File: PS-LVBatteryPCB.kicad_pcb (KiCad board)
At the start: 2 copper layers, 23.4 x 39.7 mm, 10 parts, among them J1 NTC_01, J2 NTC_02, J3 NTC_OUT, J4 SUPP+, J5 SUPP_GND, J6 SUPP_FUSE

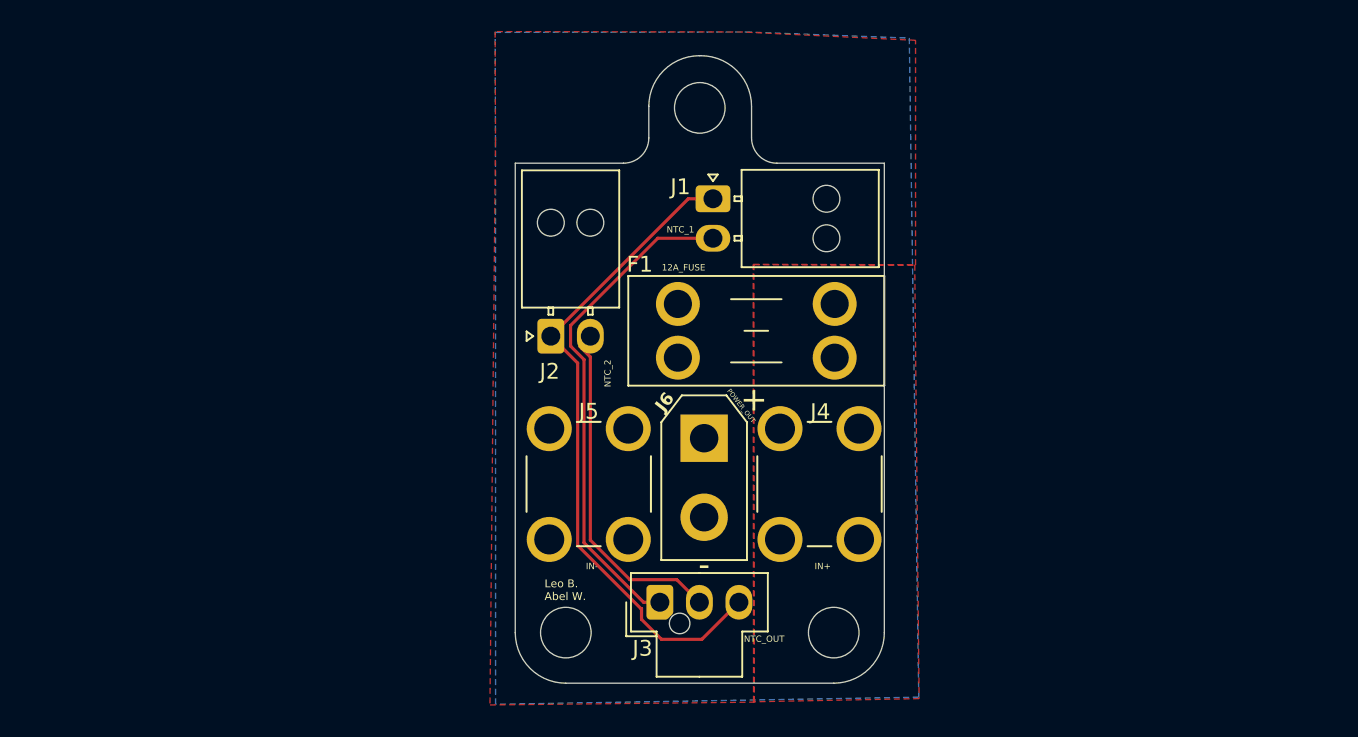
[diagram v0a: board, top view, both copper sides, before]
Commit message: redid layout for optimal terminal shape
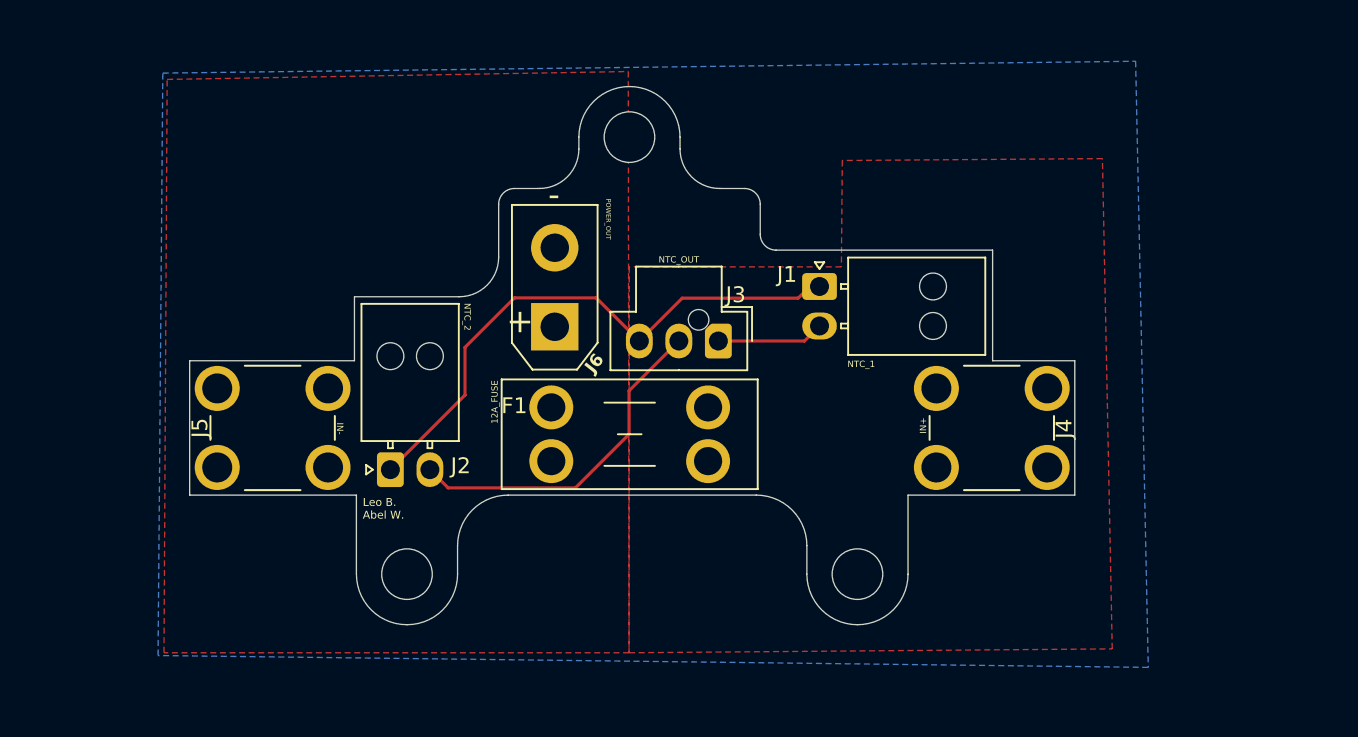
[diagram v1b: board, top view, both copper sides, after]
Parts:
- moved J5 20.3 mm to (171.1, 82.5), turned to 90 degrees
- moved J3 16.9 mm to (199.3, 77.0), turned to -90 degrees
- moved J2 13.2 mm to (178.6, 85.1)
- moved J6 11.8 mm to (188.9, 76.0), turned to 90 degrees
- moved J4 11.5 mm to (216.6, 82.5), turned to 90 degrees
- moved REF** 10.7 mm to (179.6, 91.7)
- moved F1 10.3 mm to (198.7, 84.5)
- moved J1 8.73 mm to (205.7, 73.5)
- moved REF** 4.82 mm to (193.7, 64.0)
- moved REF** 3.99 mm to (208.1, 91.7)
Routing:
- net Net-(J1-Pin_2): track 31.8 -> 6.79 mm
- net Net-(J1-Pin_1): track 41.8 -> 36.0 mm
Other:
- board size 23.4 x 39.7 mm -> 56 x 34.1 mm

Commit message: moved mounting holes
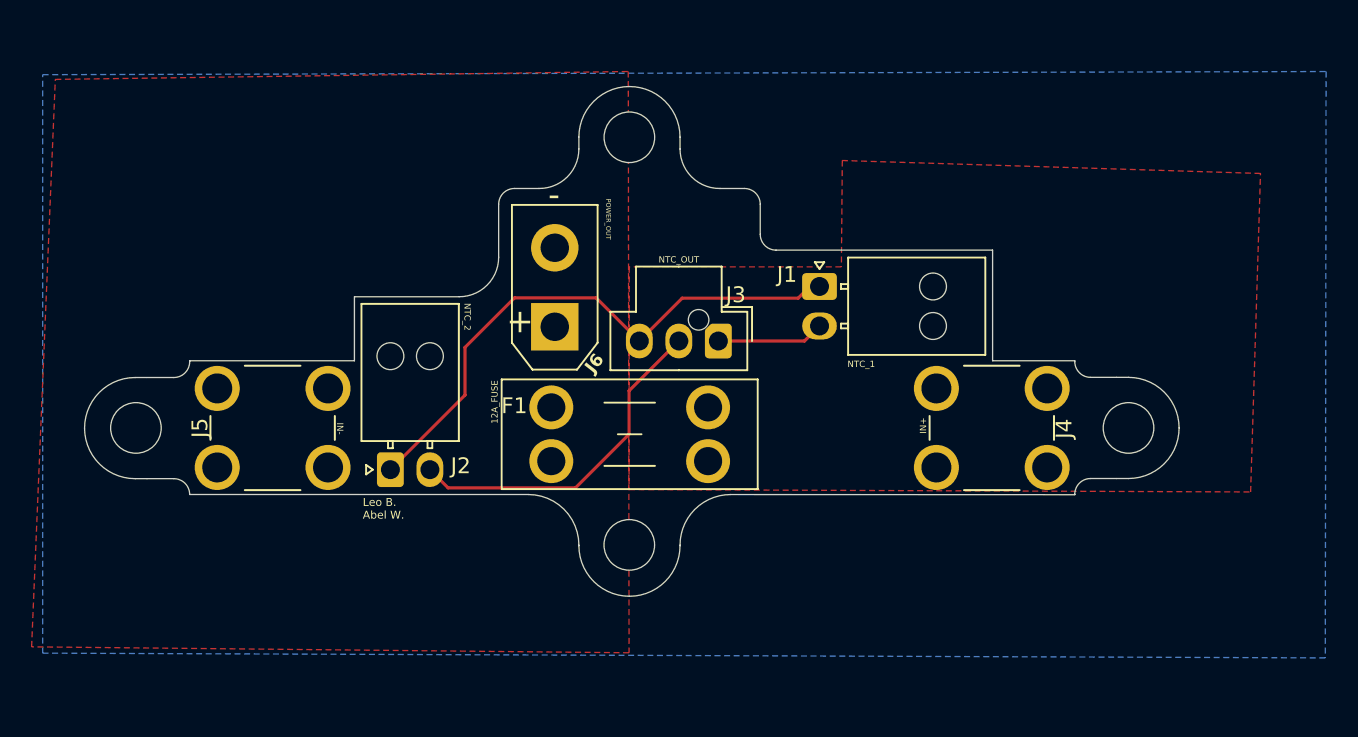
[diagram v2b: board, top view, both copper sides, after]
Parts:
- removed the REF** at (208.1, 91.7)
- added REF**: MountingHole_3.2mm_M3, MountingHole:MountingHole_3.2mm_M3, F.Cu at (193.7, 89.8)
- added REF**: MountingHole_3.2mm_M3, MountingHole:MountingHole_3.2mm_M3, F.Cu at (225.2, 82.5)
- moved REF** 19.5 mm to (162.4, 82.5), turned to 90 degrees
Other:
- board size 56 x 34.1 mm -> 69.2 x 32.2 mm

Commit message: ss fix, trace fix
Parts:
- moved REF** 0.08 mm to (193.7, 89.9)
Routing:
- net Net-(J1-Pin_1): track 36.0 -> 32.4 mm
- net Net-(J2-Pin_2): track 21.7 -> 19.6 mm
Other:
- board size 69.2 x 32.2 mm -> 69.2 x 32.3 mm

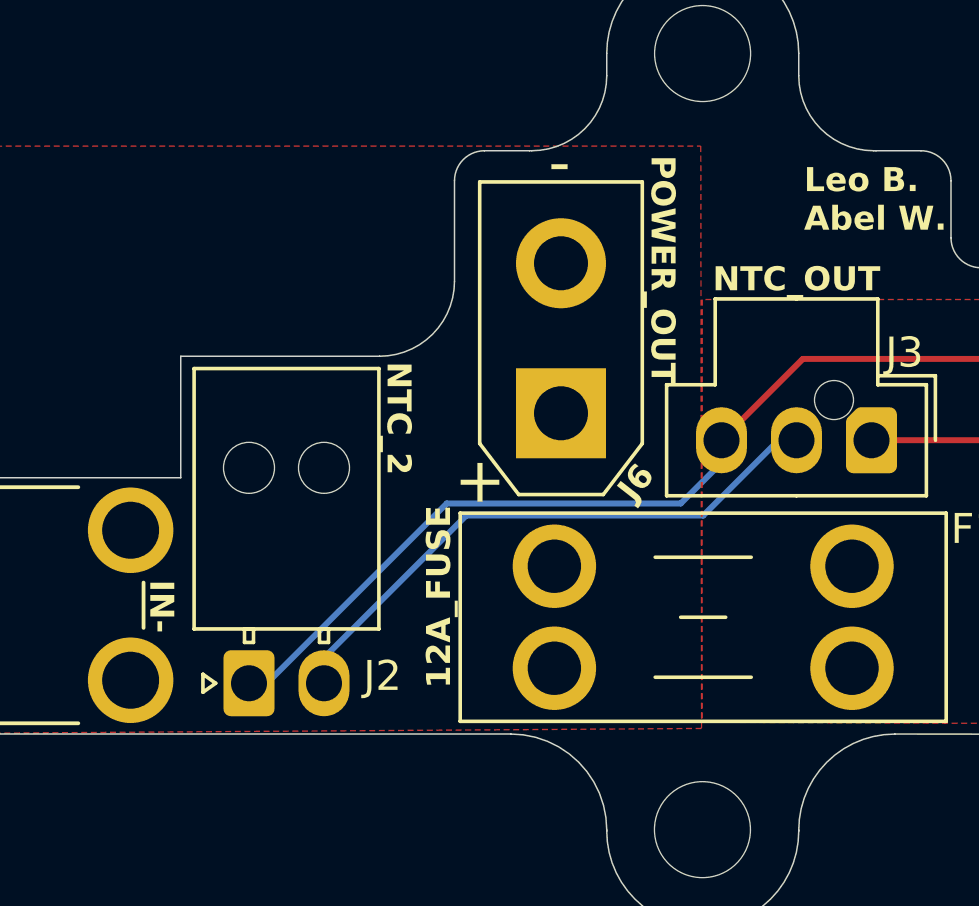
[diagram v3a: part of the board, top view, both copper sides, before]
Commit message: increased plane thickness for GND
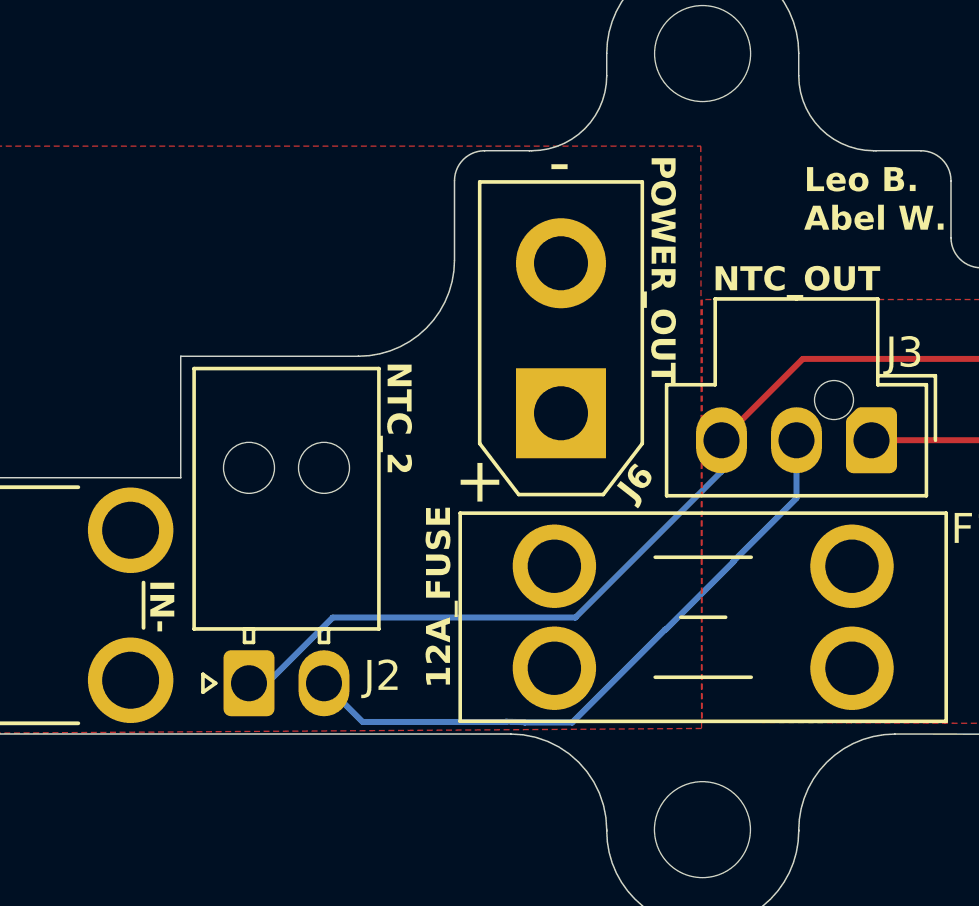
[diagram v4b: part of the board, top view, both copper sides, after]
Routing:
- net Net-(J2-Pin_2): track 19.6 -> 22.2 mm
- net Net-(J1-Pin_1): track 32.4 -> 33.1 mm
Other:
- outline, holes or cut-outs redrawn
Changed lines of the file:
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@@
+	)
+	(gr_arc
+		(start 185.4 70.95)
+		(mid 184.462742 73.212742)
+		(end 182.2 74.15)
+		(stroke
+			(width 0.05)
+			(type default)
+		)
+		(layer "Edge.Cuts")
 	)
 	(gr_arc
@@
 		(layer "Edge.Cuts")
 	)
-	(gr_arc
-		(start 185.4 71.65)
-		(mid 184.667767 73.417767)
-		(end 182.9 74.15)
-		(stroke
-			(width 0.05)
-			(type default)
-		)
-		(layer "Edge.Cuts")
-	)
 	(gr_line
 		(start 163.15 85.66)
@@
 	)
 	(gr_line
-		(start 176.275 74.15)
-		(end 182.9 74.15)
-		(stroke
-			(width 0.05)
-			(type default)
-		)
-		(layer "Edge.Cuts")
-	)
-	(gr_line
 		(start 176.275 78.2)
 		(end 176.275 74.15)
@@
 	)
 	(gr_line
-		(start 185.4 71.65)
+		(start 185.4 70.95)
 		(end 185.4 68.3)
 		(stroke
@@
 		(mid 165.557107 78.967107)
 		(end 164.85 79.26)
+		(stroke
+			(width 0.05)
+			(type default)
+		)
+		(layer "Edge.Cuts")
+	)
+	(gr_line
+		(start 176.275 74.15)
+		(end 182.2 74.15)
 		(stroke
 			(width 0.05)
@@
 	)
 	(segment
-		(start 192.942 79.058)
-		(end 194.3 77.7)
+		(start 179.15 85.05)
+		(end 181.34 82.86)
+		(width 0.2)
+		(layer "B.Cu")
+		(net 3)
+	)
+	(segment
+		(start 181.34 82.86)
+		(end 189.43 82.86)
 		(width 0.2)
 		(layer "B.Cu")
@@
 	)
 	(segment
-		(start 185.142 79.058)
-		(end 192.942 79.058)
-		(width 0.2)
-		(layer "B.Cu")
-		(net 3)
-	)
-	(segment
-		(start 194.3 77.7)
+		(start 178.55 85.05)
+		(end 179.15 85.05)
+		(width 0.2)
+		(layer "B.Cu")
+		(net 3)
+	)
+	(segment
+		(start 194.3 77.99)
 		(end 194.3 76.95)
 		(width 0.2)
@@
 	)
 	(segment
-		(start 179.11 85.09)
-		(end 185.142 79.058)
+		(start 189.43 82.86)
+		(end 194.3 77.99)
 		(width 0.2)
 		(layer "B.Cu")
@@
 	)
 	(segment
-		(start 185.791 79.459)
-		(end 181.05 84.2)
-		(width 0.2)
-		(layer "B.Cu")
-		(net 5)
-	)
-	(segment
-		(start 196.8 76.95)
-		(end 196.2 76.95)
-		(width 0.2)
-		(layer "B.Cu")
-		(net 5)
-	)
-	(segment
-		(start 196.2 76.95)
-		(end 193.691 79.459)
-		(width 0.2)
-		(layer "B.Cu")
-		(net 5)
-	)
-	(segment
-		(start 193.691 79.459)
-		(end 185.791 79.459)
+		(start 182.34057 86.34057)
+		(end 187.108501 86.341024)
+		(width 0.2)
+		(layer "B.Cu")
+		(net 5)
+	)
+	(segment
+		(start 181.05 85.05)
+		(end 182.34057 86.34057)
+		(width 0.2)
+		(layer "B.Cu")
+		(net 5)
+	)
+	(segment
+		(start 187.118597 86.33148)
+		(end 187.686085 86.347415)
+		(width 0.2)
+		(layer "B.Cu")
+		(net 5)
+	)
+	(segment
+		(start 187.108501 86.341024)
+		(end 187.118597 86.33148)
+		(width 0.2)
+		(layer "B.Cu")
+		(net 5)
+	)
+	(segment
+		(start 194.701 80.979)
+		(end 196.8 78.88)
+		(width 0.2)
+		(layer "B.Cu")
+		(net 5)
+	)
+	(segment
+		(start 194.701 80.999)
+		(end 194.701 80.979)
+		(width 0.2)
+		(layer "B.Cu")
+		(net 5)
+	)
+	(segment
+		(start 187.741204 86.36)
+		(end 189.32 86.36)
+		(width 0.2)
+		(layer "B.Cu")
+		(net 5)
+	)
+	(segment
+		(start 187.686085 86.347415)
+		(end 187.741204 86.36)
 		(width 0.2)
 		(layer "B.Cu")
@@
 		(width 0.2)
 		(layer "B.Cu")
+		(net 5)
+	)
+	(segment
+		(start 192.439 83.261)
+		(end 194.701 80.999)
+		(width 0.2)
+		(layer "B.Cu")
+		(net 5)
+	)
+	(segment
+		(start 192.419 83.261)
+		(end 192.439 83.261)
+		(width 0.2)
+		(layer "B.Cu")
+		(net 5)
+	)
+	(segment
+		(start 196.8 78.88)
+		(end 196.8 76.95)
+		(width 0.2)
+		(layer "B.Cu")
+		(net 5)
+	)
+	(segment
+		(start 189.32 86.36)
+		(end 192.419 83.261)
+		(width 0.2)
+		(layer "B.Cu")
